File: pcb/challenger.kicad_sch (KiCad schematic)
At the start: 110 parts, among them SW1 SW_Push_45deg, SW10 SW_Push_45deg, SW11 SW_Push_45deg, SW12 SW_Push_45deg, SW13 SW_Push_45deg, SW14 SW_Push_45deg, SW15 SW_Push_45deg, SW16 SW_Push_45deg, SW17 SW_Push_45deg, SW18 SW_Push_45deg, SW19 SW_Push_45deg, SW2 SW_Push_45deg, SW20 SW_Push_45deg, SW21 SW_Push_45deg, SW22 SW_Push_45deg, SW23 SW_Push_45deg, SW24 SW_Push_45deg, SW25 SW_Push_45deg, SW26 SW_Push_45deg, SW27 SW_Push_45deg, SW28 SW_Push_45deg, SW29 SW_Push_45deg, SW3 SW_Push_45deg, SW30 SW_Push_45deg, SW31 SW_Push_45deg, SW32 SW_Push_45deg, SW33 SW_Push_45deg, SW34 SW_Push_45deg, SW35 SW_Push_45deg, SW36 SW_SPDT, SW37 SW_Push, SW4 SW_Push_45deg, SW5 SW_Push_45deg, SW6 SW_Push_45deg, SW7 SW_Push_45deg, SW8 SW_Push_45deg, SW9 SW_Push_45deg, U1 ProMicro

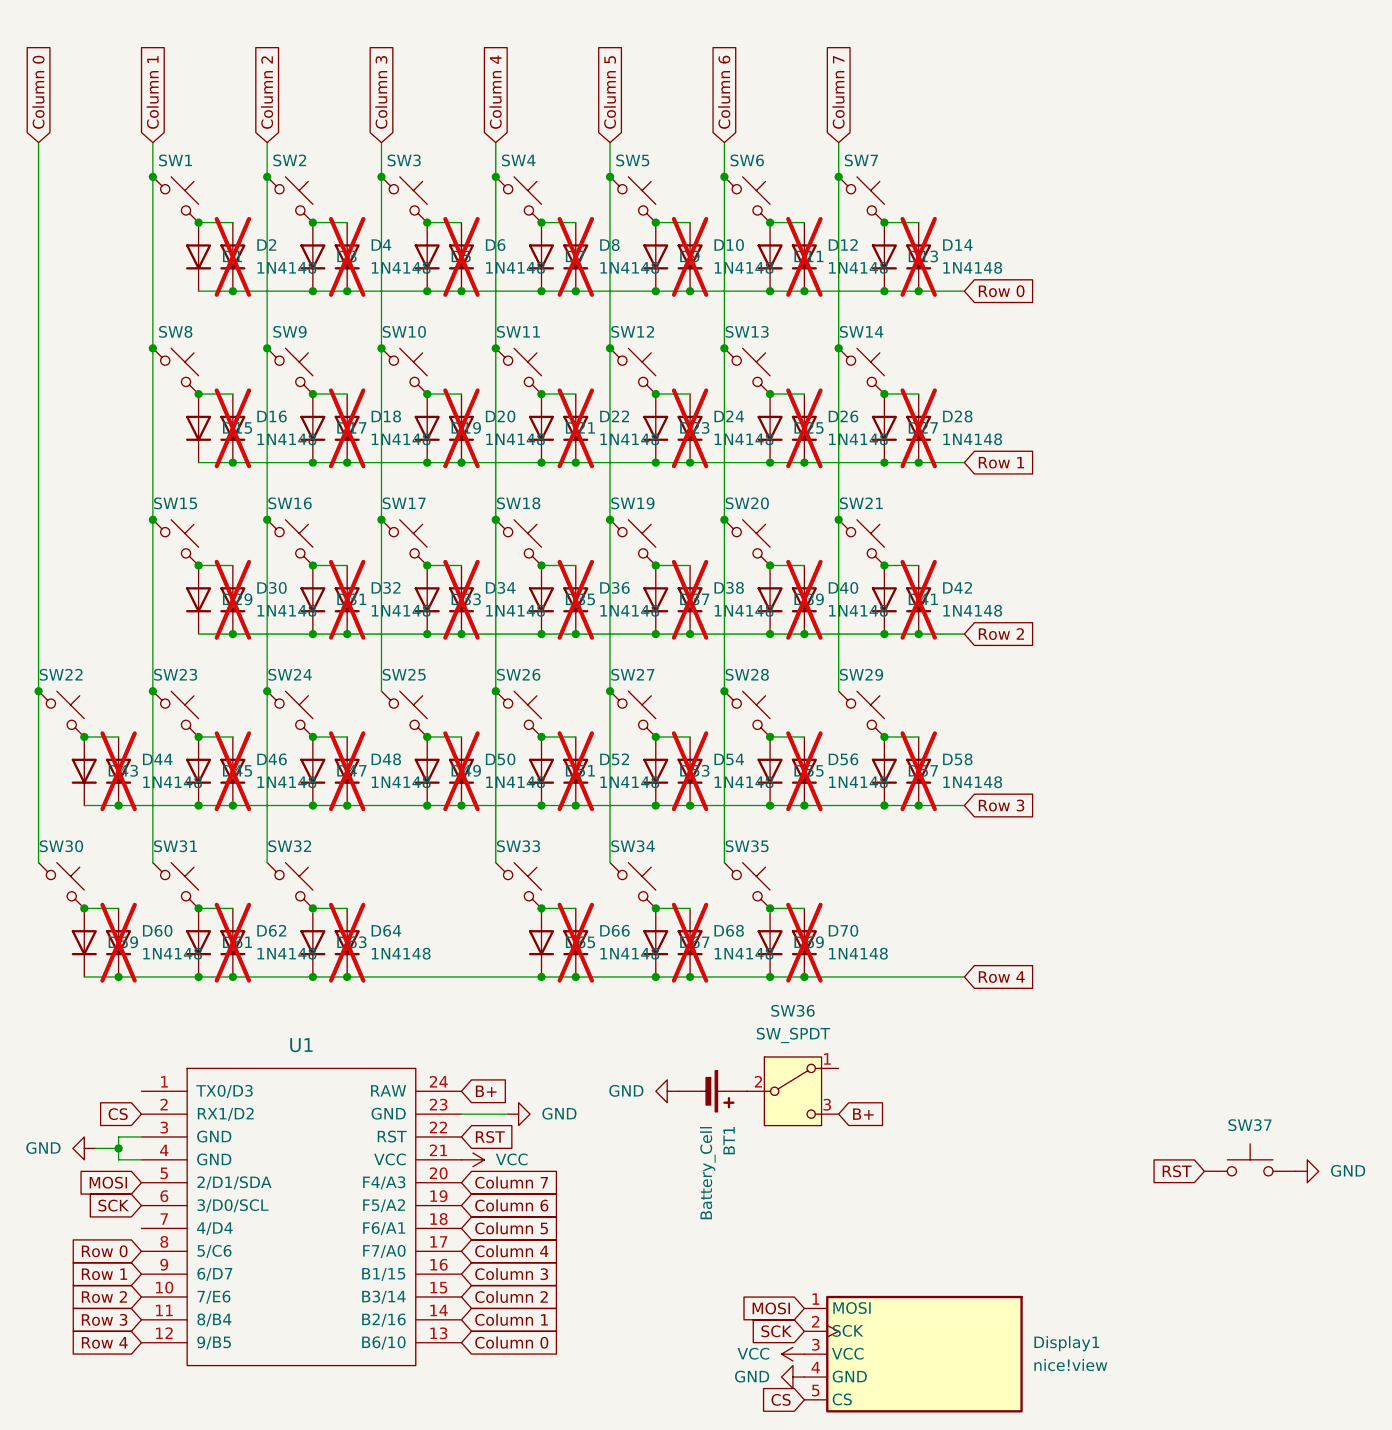
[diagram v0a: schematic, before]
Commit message: feat: remove hybrid diode setup
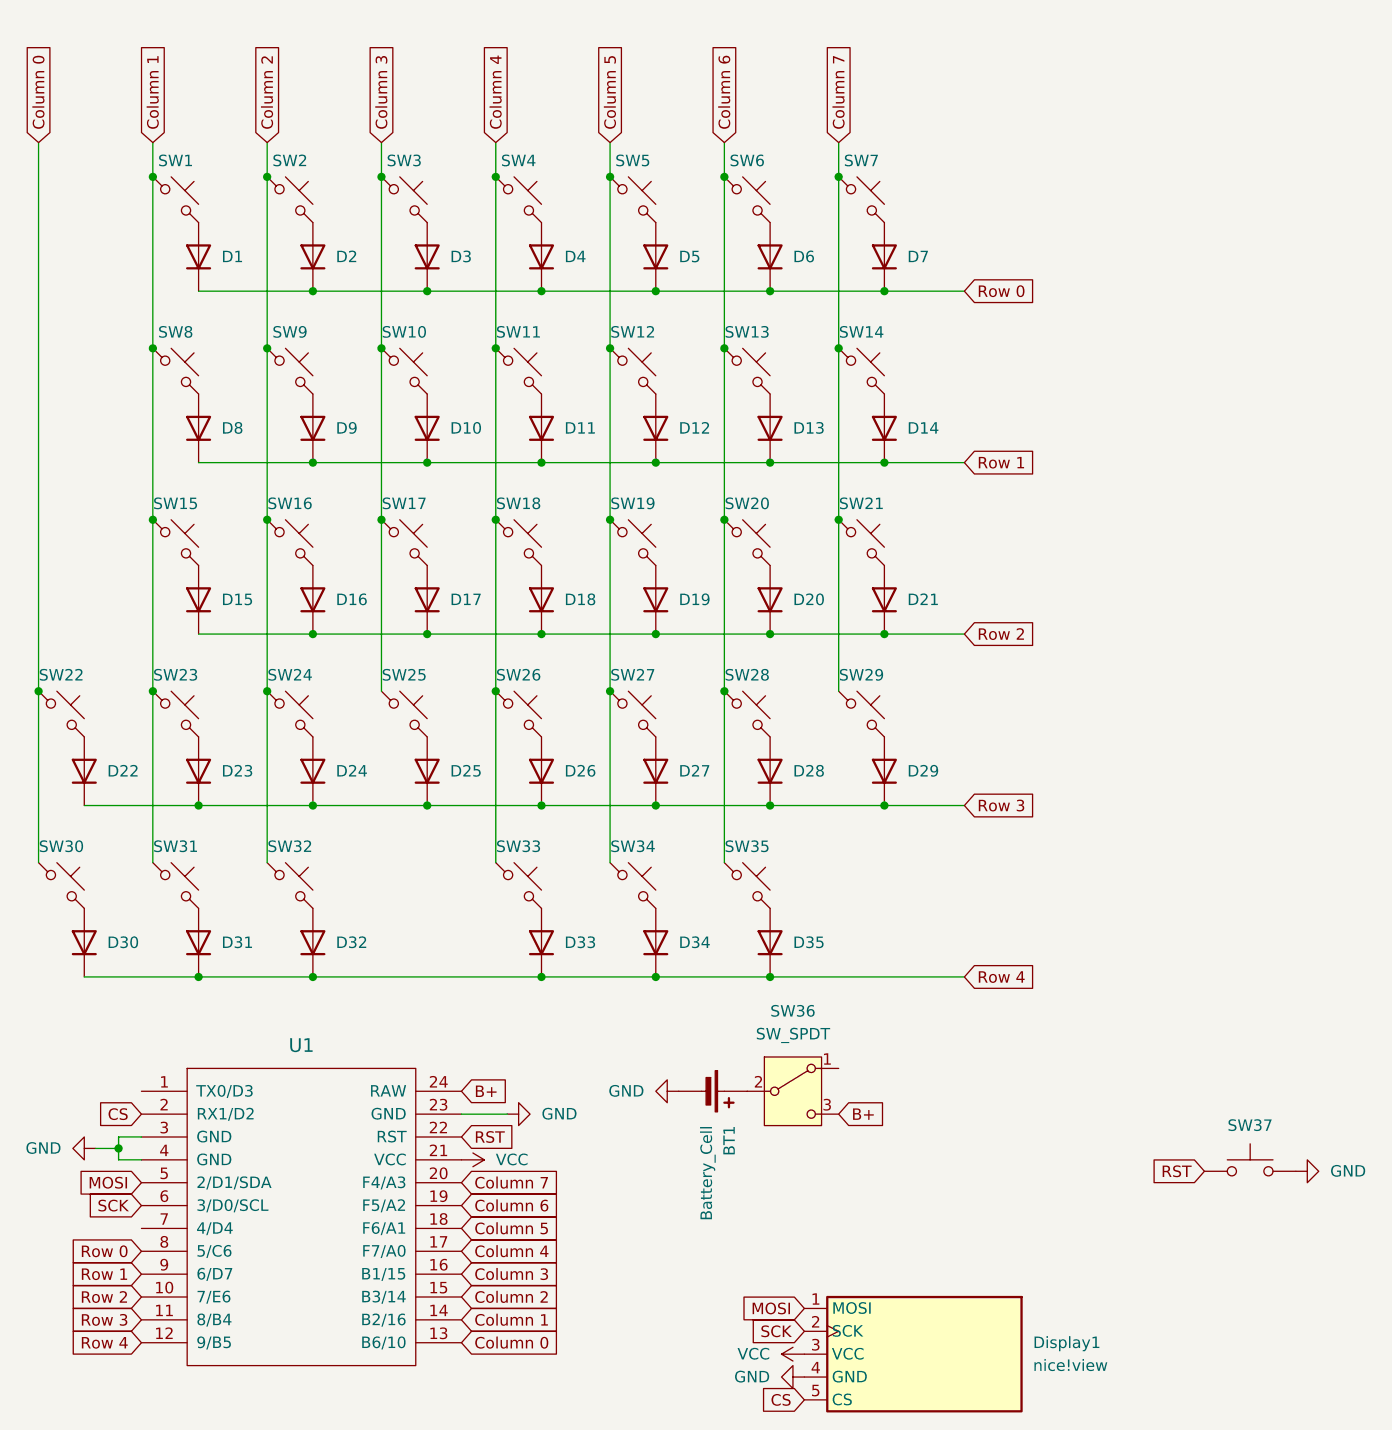
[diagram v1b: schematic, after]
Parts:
- removed D10, D12, D14, D16, D18, D2, D20, D22, D24, D26, D28, D30, D32, D34, D36, D38, D4, D40, D42, D44, D46, D48, D50, D52, D54, D56, D58, D6, D60, D62, D64, D66, D68, D70, D8: 1N4148, challenger:D_DO-35_SOD27_P7.62mm_Horizontal, symbol Diode:1N4148
- BT1: footprint Connector_JST:JST_PH_S2B-PH-K_1x02_P2.00mm_Horizontal -> challenger:JST_PH_S2B-PH-K_1x02_P2.00mm_Horizontal
- SW36: footprint Button_Switch_SMD:SW_SPDT_PCM12 -> challenger:SW_SPDT_PCM12
- SW37: footprint Button_Switch_SMD:Panasonic_EVQPUJ_EVQPUA -> challenger:Panasonic_EVQPUJ_EVQPUA
- renumbered D19 to D10, D21 to D11, D23 to D12, D25 to D13, D27 to D14, D29 to D15, D31 to D16, D33 to D17, D35 to D18, D37 to D19, D3 to D2, D39 to D20, D41 to D21, D43 to D22, D45 to D23, D47 to D24, D49 to D25, D51 to D26, D53 to D27, D55 to D28, D57 to D29, D5 to D3, D59 to D30, D61 to D31, D63 to D32, D65 to D33, D67 to D34, D69 to D35, D7 to D4, D9 to D5, D11 to D6, D13 to D7, D15 to D8, D17 to D9

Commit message: feat: update traces
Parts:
- SW37: footprint challenger:Panasonic_EVQPUJ_EVQPUA -> Button_Switch_SMD:Panasonic_EVQPUL_EVQPUC
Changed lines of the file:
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@@
 			)
 		)
-		(property "Footprint" "challenger:Panasonic_EVQPUJ_EVQPUA"
+		(property "Footprint" "Button_Switch_SMD:Panasonic_EVQPUL_EVQPUC"
 			(at 167.64 142.24 0)
 			(hide yes)

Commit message: feat: add switch and bottom plates and refine pcb
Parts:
- SW1, SW10, SW11, SW12, SW13, SW14, SW15, SW16, SW17, SW18, SW19, SW2, SW20, SW21, SW22, SW23, SW24, SW25, SW26, SW27, SW28, SW29, SW3, SW30, SW31, SW32, SW33, SW34, SW4, SW5, SW6, SW7, SW8, SW9: footprint challenger:SW_Hotswap_Kailh_MX_1.00u -> challenger:Hotswap_MX_1.00u
- SW35: footprint challenger:SW_Hotswap_Kailh_MX_1.50u -> challenger:Hotswap_MX_1.50u
- SW37: footprint Button_Switch_SMD:Panasonic_EVQPUL_EVQPUC -> challenger:Panasonic_EVQPUL_EVQPUC
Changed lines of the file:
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@@
 			)
 		)
-		(property "Footprint" "challenger:SW_Hotswap_Kailh_MX_1.00u"
+		(property "Footprint" "challenger:Hotswap_MX_1.00u"
 			(at 99.06 77.47 0)
 			(hide yes)
@@
 			)
 		)
-		(property "Footprint" "challenger:SW_Hotswap_Kailh_MX_1.00u"
+		(property "Footprint" "challenger:Hotswap_MX_1.00u"
 			(at 73.66 39.37 0)
 			(hide yes)
@@
 			)
 		)
-		(property "Footprint" "challenger:SW_Hotswap_Kailh_MX_1.00u"
+		(property "Footprint" "challenger:Hotswap_MX_1.00u"
 			(at 35.56 115.57 0)
 			(hide yes)
@@
 			)
 		)
-		(property "Footprint" "challenger:SW_Hotswap_Kailh_MX_1.00u"
+		(property "Footprint" "challenger:Hotswap_MX_1.00u"
 			(at 86.36 58.42 0)
 			(hide yes)
@@
 			)
 		)
-		(property "Footprint" "challenger:SW_Hotswap_Kailh_MX_1.00u"
+		(property "Footprint" "challenger:Hotswap_MX_1.00u"
 			(at 73.66 96.52 0)
 			(hide yes)
@@
 			)
 		)
-		(property "Footprint" "challenger:SW_Hotswap_Kailh_MX_1.00u"
+		(property "Footprint" "challenger:Hotswap_MX_1.00u"
 			(at 60.96 58.42 0)
 			(hide yes)
@@
 			)
 		)
-		(property "Footprint" "challenger:SW_Hotswap_Kailh_MX_1.00u"
+		(property "Footprint" "challenger:Hotswap_MX_1.00u"
 			(at 73.66 58.42 0)
 			(hide yes)
@@
 			)
 		)
-		(property "Footprint" "challenger:SW_Hotswap_Kailh_MX_1.00u"
+		(property "Footprint" "challenger:Hotswap_MX_1.00u"
 			(at 60.96 39.37 0)
 			(hide yes)
@@
 			)
 		)
-		(property "Footprint" "challenger:SW_Hotswap_Kailh_MX_1.00u"
+		(property "Footprint" "challenger:Hotswap_MX_1.00u"
 			(at 124.46 39.37 0)
 			(hide yes)
@@
 			)
 		)
-		(property "Footprint" "challenger:SW_Hotswap_Kailh_MX_1.00u"
+		(property "Footprint" "challenger:Hotswap_MX_1.00u"
 			(at 124.46 77.47 0)
 			(hide yes)
@@
 			)
 		)
-		(property "Footprint" "challenger:SW_Hotswap_Kailh_MX_1.00u"
+		(property "Footprint" "challenger:Hotswap_MX_1.00u"
 			(at 99.06 39.37 0)
 			(hide yes)
@@
 			)
 		)
-		(property "Footprint" "challenger:SW_Hotswap_Kailh_MX_1.00u"
+		(property "Footprint" "challenger:Hotswap_MX_1.00u"
 			(at 124.46 58.42 0)
 			(hide yes)
@@
 			)
 		)
-		(property "Footprint" "Button_Switch_SMD:Panasonic_EVQPUL_EVQPUC"
+		(property "Footprint" "challenger:Panasonic_EVQPUL_EVQPUC"
 			(at 167.64 142.24 0)
 			(hide yes)
@@
 			)
 		)
-		(property "Footprint" "challenger:SW_Hotswap_Kailh_MX_1.00u"
+		(property "Footprint" "challenger:Hotswap_MX_1.00u"
 			(at 99.06 115.57 0)
 			(hide yes)
@@
 			)
 		)
-		(property "Footprint" "challenger:SW_Hotswap_Kailh_MX_1.00u"
+		(property "Footprint" "challenger:Hotswap_MX_1.00u"
 			(at 60.96 115.57 0)
 			(hide yes)
@@
 			)
 		)
-		(property "Footprint" "challenger:SW_Hotswap_Kailh_MX_1.00u"
+		(property "Footprint" "challenger:Hotswap_MX_1.00u"
 			(at 124.46 96.52 0)
 			(hide yes)
@@
 			)
 		)
-		(property "Footprint" "challenger:SW_Hotswap_Kailh_MX_1.50u"
+		(property "Footprint" "challenger:Hotswap_MX_1.50u"
 			(at 111.76 115.57 0)
 			(hide yes)
@@
 			)
 		)
-		(property "Footprint" "challenger:SW_Hotswap_Kailh_MX_1.00u"
+		(property "Footprint" "challenger:Hotswap_MX_1.00u"
 			(at 60.96 77.47 0)
 			(hide yes)
@@
 			)
 		)
-		(property "Footprint" "challenger:SW_Hotswap_Kailh_MX_1.00u"
+		(property "Footprint" "challenger:Hotswap_MX_1.00u"
 			(at 86.36 77.47 0)
 			(hide yes)
@@
 			)
 		)
-		(property "Footprint" "challenger:SW_Hotswap_Kailh_MX_1.00u"
+		(property "Footprint" "challenger:Hotswap_MX_1.00u"
 			(at 35.56 96.52 0)
 			(hide yes)
@@
 			)
 		)
-		(property "Footprint" "challenger:SW_Hotswap_Kailh_MX_1.00u"
+		(property "Footprint" "challenger:Hotswap_MX_1.00u"
 			(at 48.26 58.42 0)
 			(hide yes)
@@
 			)
 		)
-		(property "Footprint" "challenger:SW_Hotswap_Kailh_MX_1.00u"
+		(property "Footprint" "challenger:Hotswap_MX_1.00u"
 			(at 111.76 39.37 0)
 			(hide yes)
@@
 			)
 		)
-		(property "Footprint" "challenger:SW_Hotswap_Kailh_MX_1.00u"
+		(property "Footprint" "challenger:Hotswap_MX_1.00u"
 			(at 111.76 77.47 0)
 			(hide yes)
@@
 			)
 		)
-		(property "Footprint" "challenger:SW_Hotswap_Kailh_MX_1.00u"
+		(property "Footprint" "challenger:Hotswap_MX_1.00u"
 			(at 86.36 39.37 0)
 			(hide yes)
@@
 			)
 		)
-		(property "Footprint" "challenger:SW_Hotswap_Kailh_MX_1.00u"
+		(property "Footprint" "challenger:Hotswap_MX_1.00u"
 			(at 48.26 96.52 0)
 			(hide yes)
@@
 			)
 		)
-		(property "Footprint" "challenger:SW_Hotswap_Kailh_MX_1.00u"
+		(property "Footprint" "challenger:Hotswap_MX_1.00u"
 			(at 48.26 77.47 0)
 			(hide yes)
@@
 			)
 		)
-		(property "Footprint" "challenger:SW_Hotswap_Kailh_MX_1.00u"
+		(property "Footprint" "challenger:Hotswap_MX_1.00u"
 			(at 48.26 39.37 0)
 			(hide yes)
@@
 			)
 		)
-		(property "Footprint" "challenger:SW_Hotswap_Kailh_MX_1.00u"
+		(property "Footprint" "challenger:Hotswap_MX_1.00u"
 			(at 86.36 115.57 0)
 			(hide yes)
@@
 			)
 		)
-		(property "Footprint" "challenger:SW_Hotswap_Kailh_MX_1.00u"
+		(property "Footprint" "challenger:Hotswap_MX_1.00u"
 			(at 111.76 58.42 0)
 			(hide yes)
@@
 			)
 		)
-		(property "Footprint" "challenger:SW_Hotswap_Kailh_MX_1.00u"
+		(property "Footprint" "challenger:Hotswap_MX_1.00u"
 			(at 111.76 96.52 0)
 			(hide yes)
@@
 			)
 		)
-		(property "Footprint" "challenger:SW_Hotswap_Kailh_MX_1.00u"
+		(property "Footprint" "challenger:Hotswap_MX_1.00u"
 			(at 60.96 96.52 0)
 			(hide yes)
@@
 			)
 		)
-		(property "Footprint" "challenger:SW_Hotswap_Kailh_MX_1.00u"
+		(property "Footprint" "challenger:Hotswap_MX_1.00u"
 			(at 86.36 96.52 0)
 			(hide yes)
@@
 			)
 		)
-		(property "Footprint" "challenger:SW_Hotswap_Kailh_MX_1.00u"
+		(property "Footprint" "challenger:Hotswap_MX_1.00u"
 			(at 99.06 96.52 0)
 			(hide yes)
@@
 			)
 		)
-		(property "Footprint" "challenger:SW_Hotswap_Kailh_MX_1.00u"
+		(property "Footprint" "challenger:Hotswap_MX_1.00u"
 			(at 73.66 77.47 0)
 			(hide yes)
@@
 			)
 		)
-		(property "Footprint" "challenger:SW_Hotswap_Kailh_MX_1.00u"
+		(property "Footprint" "challenger:Hotswap_MX_1.00u"
 			(at 48.26 115.57 0)
 			(hide yes)
@@
 			)
 		)
-		(property "Footprint" "challenger:SW_Hotswap_Kailh_MX_1.00u"
+		(property "Footprint" "challenger:Hotswap_MX_1.00u"
 			(at 99.06 58.42 0)
 			(hide yes)
